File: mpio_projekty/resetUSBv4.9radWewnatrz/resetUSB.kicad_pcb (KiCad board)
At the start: 2 copper layers, 39 x 180 mm, 58 parts, among them J1 USBB-G-SMD, J10 FC68391, J2 TUEA4F2SOBHT, J3 Conn_02x05, J4 SWD_4pin, J5 Conn_02x05, J6 Conn_02x05, J7 AC3MAH-AU-PRE, J8 Mini-Fit Jr; 4,2mm, J9 FC68391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

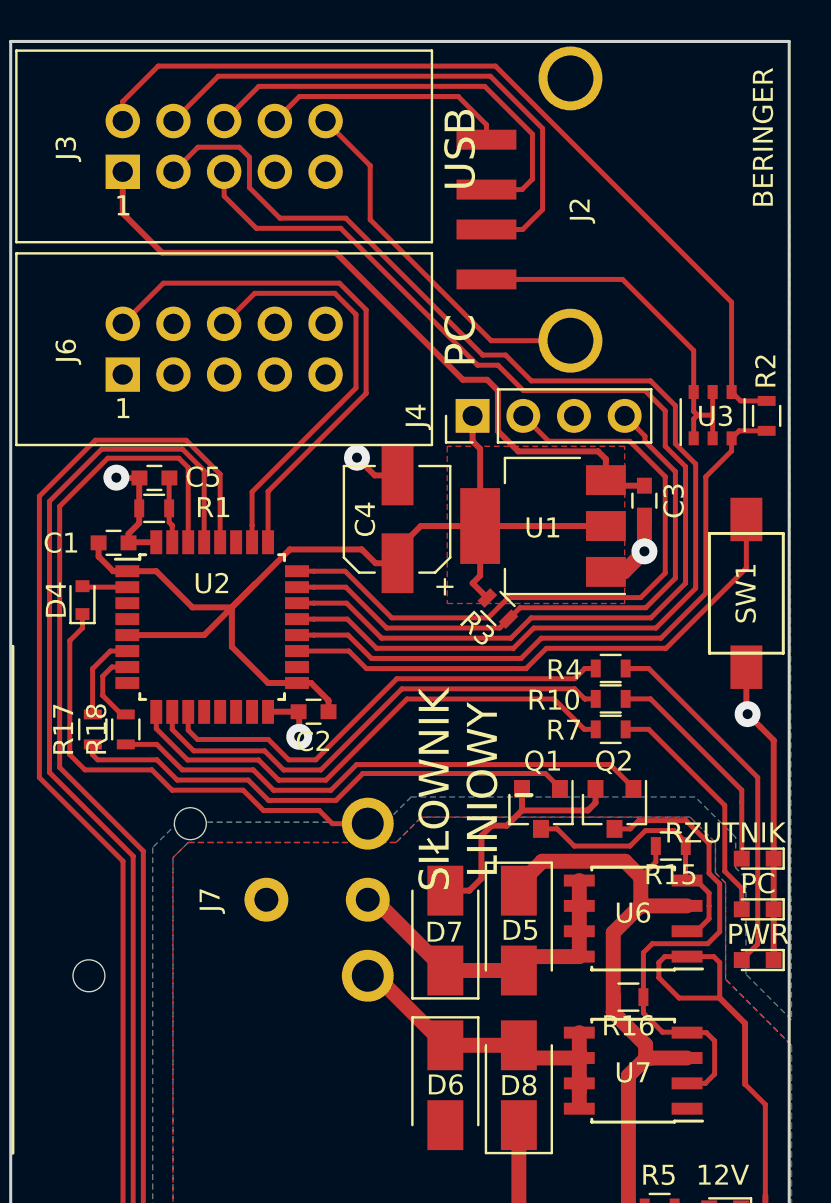
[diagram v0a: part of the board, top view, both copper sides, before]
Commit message: resetUSBradWewnatrz,Zewnatrz, AGND bez przelotek.
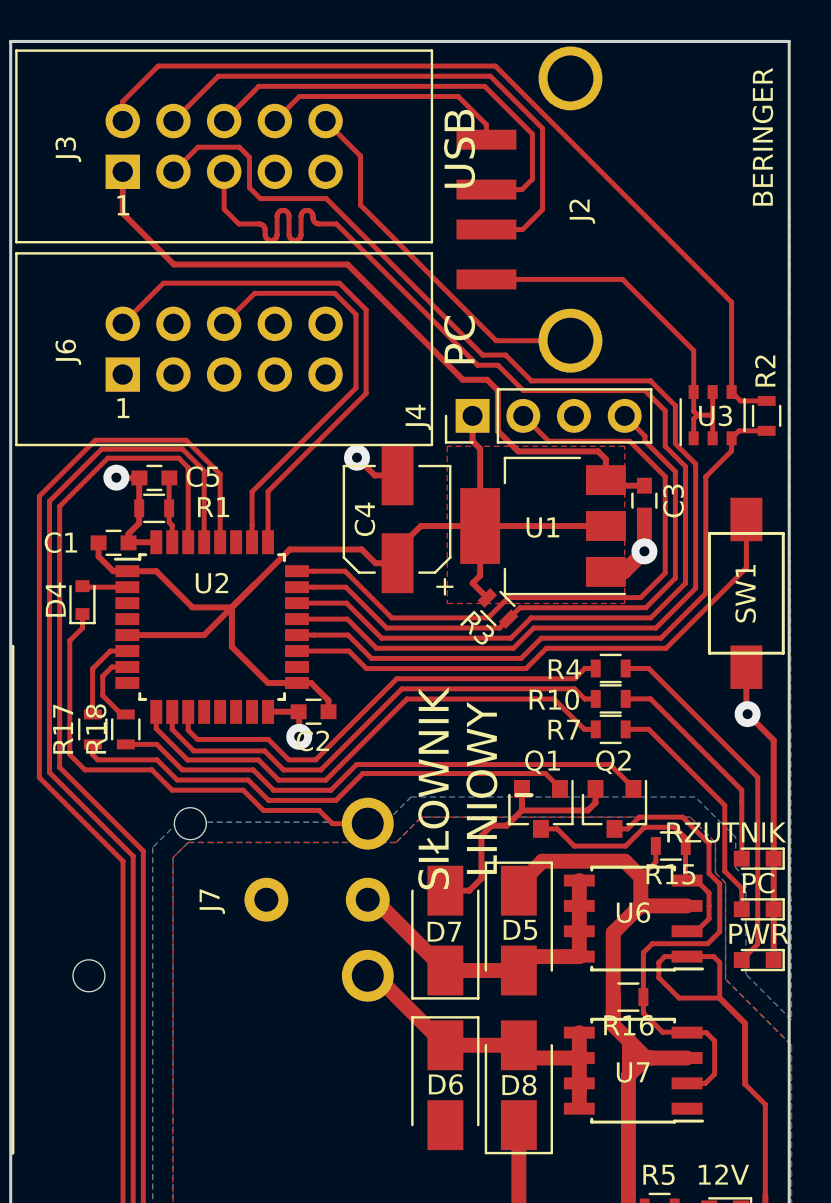
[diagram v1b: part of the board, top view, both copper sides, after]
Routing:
- net /USB_P: track 58.2 -> 63.3 mm
- net +12V: track 296.8 -> 298.5 mm
